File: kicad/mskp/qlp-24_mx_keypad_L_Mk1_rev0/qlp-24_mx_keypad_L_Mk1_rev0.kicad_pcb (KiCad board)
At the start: 2 copper layers, 162 x 112 mm, 30 parts, among them J1 Conn_01x12_Socket, SW1 Switch, SW10 Switch, SW11 Switch, SW12 Switch, SW2 Switch, SW3 Switch, SW4 Switch, SW5 Switch, SW6 Switch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

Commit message: Minor keypad design update ideas
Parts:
- added REF**: MountingHole_2.2mm_M2_ISO14580, MountingHole:MountingHole_2.2mm_M2_ISO14580, F.Cu at (101.2, 63.5)
- moved D6 23.9 mm to (83.4, 43.0)
- moved D9 12.2 mm to (111.0, 62.2)
- moved D3 6.10 mm to (203.4, 126.9)
- moved SW11 6.10 mm to (151.0, 76.0)
- moved D5 6.10 mm to (143.4, 47.2)
- moved SW5 6.10 mm to (151.0, 56.0)
- moved D1 6.10 mm to (163.4, 107.1)
- moved D11 6.10 mm to (143.4, 67.1)
- moved D12 6.10 mm to (163.4, 61.9)
- moved D2 6.10 mm to (183.4, 112.2)
- moved D7 6.10 mm to (63.4, 77.2)
- moved G*** 6.10 mm to (175.9, 85.3)
- moved H3 6.10 mm to (163.8, 103.1)
- moved J1 6.10 mm to (179.1, 93.6)
- moved SW1 6.10 mm to (171.0, 116.0)
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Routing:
- net Net-(D9-A): track 12.6 -> 0.00 mm

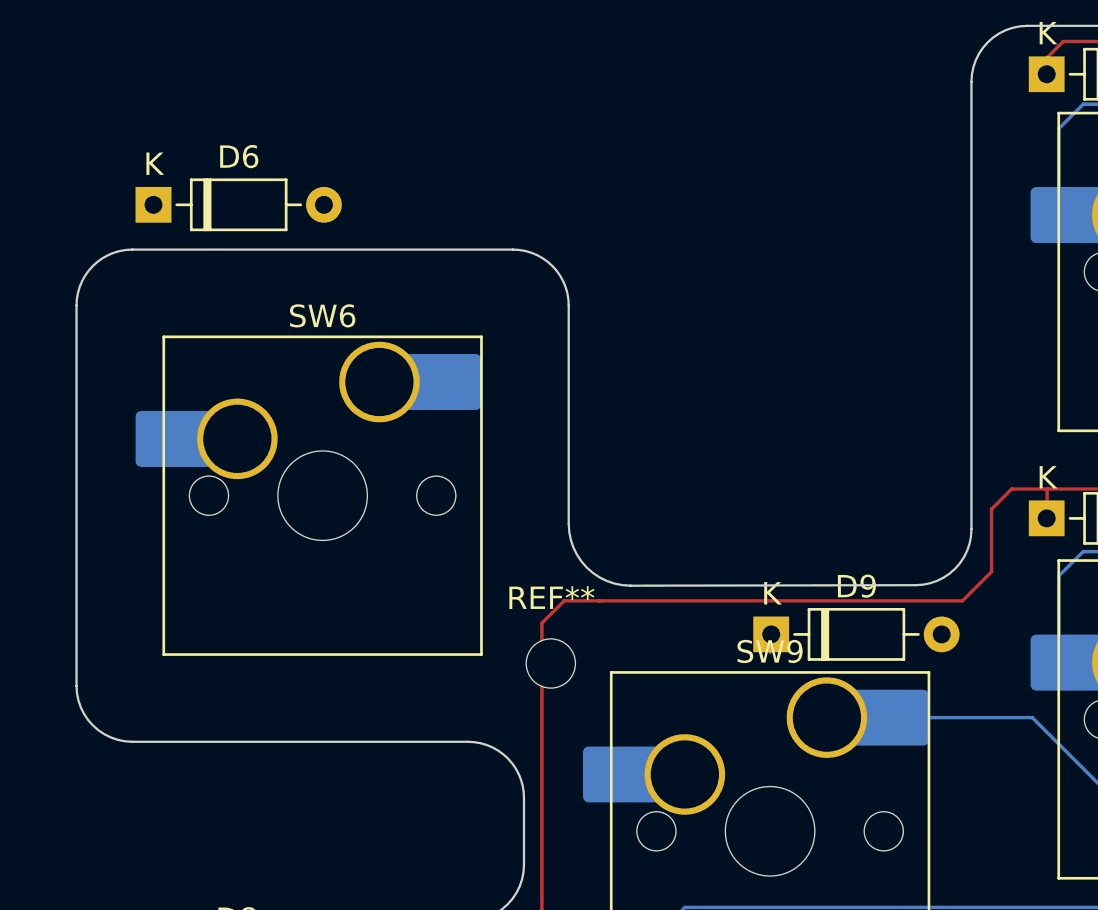
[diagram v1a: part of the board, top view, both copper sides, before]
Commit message: Minor pcb updates for qlp and seok keypads
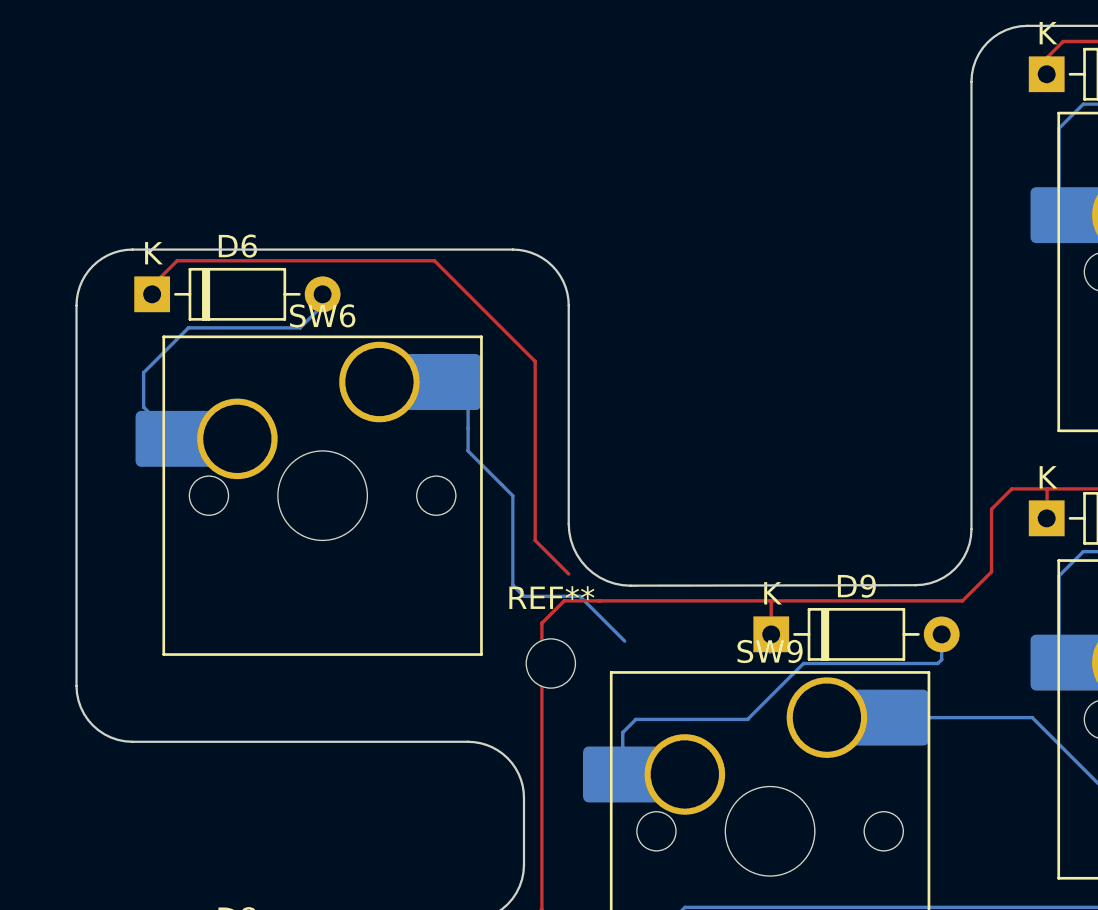
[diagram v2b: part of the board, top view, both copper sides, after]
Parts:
- moved D6 4.00 mm to (83.4, 47.0)
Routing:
- net Net-(D1-K): track 184.8 -> 214.8 mm
- net Net-(D9-A): track 0.00 -> 18.6 mm
- net Net-(J1-Pin_7): track 43.7 -> 60.1 mm
- net Net-(D6-A): track 0.00 -> 13.3 mm
- net Net-(D10-K): track 170.8 -> 172.3 mm
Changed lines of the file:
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@@
   )
   (footprint "Diode_THT:D_DO-35_SOD27_P7.62mm_Horizontal" (layer "F.Cu")
-    (at 83.440002 43)
+    (at 83.379998 47)
     (descr "Diode, DO-35_SOD27 series, Axial, Horizontal, pin pitch=7.62mm, , length*diameter=4*2mm^2, , http://www.diodes.com/_files/packages/DO-35.pdf")
     (tags "Diode DO-35_SOD27 series Axial Horizontal pin pitch 7.62mm  length 4mm diameter 2mm")
@@
   (segment (start 99.600001 75.700002) (end 100.800001 74.500002) (width 0.15) (layer "F.Cu") (net 5))
   (segment (start 140.900002 65.699999) (end 143.400002 65.700003) (width 0.15) (layer "F.Cu") (net 5))
+  (segment (start 111.05 60.75) (end 111 60.7) (width 0.15) (layer "F.Cu") (net 5))
   (segment (start 64.680002 75.700002) (end 64.880001 75.7) (width 0.15) (layer "F.Cu") (net 5))
   (segment (start 161.200002 62.800002) (end 162.000001 62) (width 0.15) (layer "F.Cu") (net 5))
@@
   (segment (start 160.600001 65.700001) (end 161.2 66.300001) (width 0.15) (layer "F.Cu") (net 5))
   (segment (start 120.900001 56.600001) (end 121.800001 55.700001) (width 0.15) (layer "F.Cu") (net 5))
+  (segment (start 111 60.7) (end 119.600002 60.7) (width 0.15) (layer "F.Cu") (net 5))
   (segment (start 123.380001 56.999999) (end 123.38 55.719999) (width 0.15) (layer "F.Cu") (net 5))
   (segment (start 100.800001 74.500002) (end 100.800002 61.699999) (width 0.15) (layer "F.Cu") (net 5))
+  (segment (start 111.05 62.2) (end 111.05 60.75) (width 0.15) (layer "F.Cu") (net 5))
   (segment (start 83.38 77) (end 83.38 75.720001) (width 0.15) (layer "F.Cu") (net 5))
   (segment (start 161.200003 67) (end 161.200002 85.000002) (width 0.15) (layer "F.Cu") (net 5))
@@
   (segment (start 139.8 59.800002) (end 139.800001 64.6) (width 0.15) (layer "F.Cu") (net 5))
   (segment (start 83.400002 75.700001) (end 99.600001 75.700002) (width 0.15) (layer "F.Cu") (net 5))
-  (segment (start 103.400002 60.7) (end 119.600002 60.7) (width 0.15) (layer "F.Cu") (net 5))
   (segment (start 143.400002 65.700003) (end 160.600001 65.700001) (width 0.15) (layer "F.Cu") (net 5))
   (segment (start 123.38 55.719999) (end 123.400002 55.700001) (width 0.15) (layer "F.Cu") (net 5))
   (segment (start 120.900002 59.400001) (end 120.900001 56.600001) (width 0.15) (layer "F.Cu") (net 5))
   (segment (start 162.000001 62) (end 163.380001 62.000001) (width 0.15) (layer "F.Cu") (net 5))
+  (segment (start 103.400002 60.7) (end 111 60.7) (width 0.15) (layer "F.Cu") (net 5))
   (segment (start 121.800001 55.700001) (end 123.400002 55.700001) (width 0.15) (layer "F.Cu") (net 5))
   (segment (start 101.800003 60.7) (end 103.400002 60.7) (width 0.15) (layer "F.Cu") (net 5))
@@
   (segment (start 143.914999 53.460002) (end 143.914998 49.585002) (width 0.15) (layer "B.Cu") (net 6))
   (segment (start 150.500001 48.500001) (end 151 48.000003) (width 0.15) (layer "B.Cu") (net 6))
+  (segment (start 84.414998 53.459999) (end 83 52.045001) (width 0.15) (layer "B.Cu") (net 7))
+  (segment (start 83 50.5) (end 85 48.5) (width 0.15) (layer "B.Cu") (net 7))
+  (segment (start 90.999998 47.500002) (end 90.999998 47) (width 0.15) (layer "B.Cu") (net 7))
+  (segment (start 90 48.5) (end 90.999998 47.500002) (width 0.15) (layer "B.Cu") (net 7))
+  (segment (start 83 52.045001) (end 83 50.5) (width 0.15) (layer "B.Cu") (net 7))
+  (segment (start 85 48.5) (end 90 48.5) (width 0.15) (layer "B.Cu") (net 7))
   (segment (start 71.000001 78) (end 71 77) (width 0.15) (layer "B.Cu") (net 8))
   (segment (start 63.915001 83.460001) (end 63.915002 79.585003) (width 0.15) (layer "B.Cu") (net 8))
@@
   (segment (start 90.500002 78.500001) (end 90.999999 78.000002) (width 0.15) (layer "B.Cu") (net 9))
   (segment (start 83.915 79.585002) (end 85.000002 78.5) (width 0.15) (layer "B.Cu") (net 9))
+  (segment (start 118.67 63.33) (end 118.5 63.5) (width 0.15) (layer "B.Cu") (net 10))
+  (segment (start 104.414998 66.585002) (end 104.414998 68.459999) (width 0.15) (layer "B.Cu") (net 10))
+  (segment (start 112.5 63.5) (end 110 66) (width 0.15) (layer "B.Cu") (net 10))
+  (segment (start 105 66) (end 104.414998 66.585002) (width 0.15) (layer "B.Cu") (net 10))
+  (segment (start 110 66) (end 105 66) (width 0.15) (layer "B.Cu") (net 10))
+  (segment (start 118.5 63.5) (end 112.5 63.5) (width 0.15) (layer "B.Cu") (net 10))
+  (segment (start 118.67 62.2) (end 118.67 63.33) (width 0.15) (layer "B.Cu") (net 10))
   (segment (start 125.000003 58.500002) (end 130.5 58.5) (width 0.15) (layer "B.Cu") (net 11))
   (segment (start 123.915002 63.460003) (end 123.915001 59.585001) (width 0.15) (layer "B.Cu") (net 11))
@@
   (segment (start 123.915001 59.585001) (end 125.000003 58.500002) (width 0.15) (layer "B.Cu") (net 11))
   (segment (start 131 58.000002) (end 131.000001 57.000003) (width 0.15) (layer "B.Cu") (net 11))
+  (segment (start 100 60.5) (end 101 60.5) (width 0.15) (layer "B.Cu") (net 16))
   (segment (start 171.550002 94.25) (end 177.250001 94.249999) (width 0.15) (layer "B.Cu") (net 16))
+  (segment (start 99.5 56) (end 99.5 60) (width 0.15) (layer "B.Cu") (net 16))
+  (segment (start 97.5 54) (end 99 55.5) (width 0.15) (layer "B.Cu") (net 16))
   (segment (start 179.100003 81.099999) (end 177.100003 83.100001) (width 0.15) (layer "B.Cu") (net 16))
+  (segment (start 97.5 52.100001) (end 97.5 53) (width 0.15) (layer "B.Cu") (net 16))
+  (segment (start 101 60.5) (end 102.5 60.5) (width 0.15) (layer "B.Cu") (net 16))
+  (segment (start 97.5 53) (end 97.5 54) (width 0.15) (layer "B.Cu") (net 16))
+  (segment (start 96.319998 50.919999) (end 97.5 52.100001) (width 0.15) (layer "B.Cu") (net 16))
   (segment (start 170.400001 83.100001) (end 169.500002 84.000001) (width 0.15) (layer "B.Cu") (net 16))
+  (segment (start 102.5 60.5) (end 104.5 62.5) (width 0.15) (layer "B.Cu") (net 16))
   (segment (start 176.841999 67.841997) (end 179.100002 70.100002) (width 0.15) (layer "B.Cu") (net 16))
   (segment (start 169.500002 84.000001) (end 169.5 92.2) (width 0.15) (layer "B.Cu") (net 16))
@@
   (segment (start 177.100003 83.100001) (end 170.400001 83.100001) (width 0.15) (layer "B.Cu") (net 16))
   (segment (start 176.842 65.92) (end 176.841999 67.841997) (width 0.15) (layer "B.Cu") (net 16))
+  (segment (start 99 55.5) (end 99.5 56) (width 0.15) (layer "B.Cu") (net 16))
   (segment (start 179.100002 70.100002) (end 179.100003 81.099999) (width 0.15) (layer "B.Cu") (net 16))
+  (segment (start 99.5 60) (end 100 60.5) (width 0.15) (layer "B.Cu") (net 16))
   (segment (start 158.980001 70.920003) (end 159.000003 70.9) (width 0.15) (layer "B.Cu") (net 17))
   (segment (start 159.000003 70.9) (end 159.000001 53.078002) (width 0.15) (layer "B.Cu") (net 17))
@@
   (segment (start 165.600001 94.100001) (end 169.100001 97.600001) (width 0.15) (layer "B.Cu") (net 21))
   (segment (start 183.38 110.720001) (end 183.400002 110.700001) (width 0.15) (layer "F.Cu") (net 22))
+  (segment (start 84.5 45.5) (end 96 45.5) (width 0.15) (layer "F.Cu") (net 22))
   (segment (start 200.000001 112.100001) (end 198.600002 110.7) (width 0.15) (layer "F.Cu") (net 22))
   (segment (start 181.300002 110.700001) (end 179.800002 109.200001) (width 0.15) (layer "F.Cu") (net 22))
@@
   (segment (start 200.000002 126.1) (end 200.000001 112.100001) (width 0.15) (layer "F.Cu") (net 22))
   (segment (start 161.800002 86.800002) (end 172.100002 86.799999) (width 0.15) (layer "F.Cu") (net 22))
+  (segment (start 100.5 58) (end 102 59.5) (width 0.15) (layer "F.Cu") (net 22))
   (segment (start 200.900001 126.999999) (end 200.000002 126.1) (width 0.15) (layer "F.Cu") (net 22))
+  (segment (start 83.379998 46.620002) (end 84.5 45.5) (width 0.15) (layer "F.Cu") (net 22))
+  (segment (start 83.379998 47) (end 83.379998 46.620002) (width 0.15) (layer "F.Cu") (net 22))
   (segment (start 143.379998 47) (end 143.380001 45.820002) (width 0.15) (layer "F.Cu") (net 22))
   (segment (start 123.400001 36.400001) (end 124.1 35.7) (width 0.15) (layer "F.Cu") (net 22))
@@
   (segment (start 143.400001 45.799999) (end 153.600003 45.800001) (width 0.15) (layer "F.Cu") (net 22))
   (segment (start 179.800001 106.200001) (end 179.300002 105.7) (width 0.15) (layer "F.Cu") (net 22))
+  (segment (start 96 45.5) (end 100.5 50) (width 0.15) (layer "F.Cu") (net 22))
   (segment (start 161 104.400001) (end 161.000001 87.599998) (width 0.15) (layer "F.Cu") (net 22))
+  (segment (start 100.5 50) (end 100.5 58) (width 0.15) (layer "F.Cu") (net 22))
   (segment (start 124.1 35.7) (end 139.500004 35.7) (width 0.15) (layer "F.Cu") (net 22))
   (segment (start 141.800002 45.8) (end 143.400001 45.799999) (width 0.15) (layer "F.Cu") (net 22))
